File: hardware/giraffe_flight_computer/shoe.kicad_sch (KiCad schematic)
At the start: 65 parts, among them J8 USB, J9 EXT_AUDIO, U10 PCM2902C, U11 TPS61033, U12 ISO6720B, U14 74LVC1G04, U15 TLP185, U16 TLP185, Y1 12MHz

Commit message: first round of updates to telemetry board
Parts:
- removed C38: 10μF, Capacitor_Tantalum_SMD:CP_EIA-3216-18_Kemet-A, symbol Device:C_Polarized_Small
- removed C45: 100μF, Capacitor_Tantalum_SMD:CP_EIA-7343-31_Kemet-D, symbol Device:C_Polarized_Small
- removed L2: 0.47uH, Inductor_SMD:L_Coilcraft_XAL4020-XXX, symbol Device:L_Small
- removed R19: ?k, Potentiometer_SMD:Potentiometer_Bourns_TC33X_Vertical, symbol giraffe_symbols:R_Potentiometer
- removed R20: ?Ω, Resistor_SMD:R_0603_1608Metric, symbol Device:R_Small
- removed R33, R35: ?k, Resistor_SMD:R_0603_1608Metric, symbol Device:R_Small
- removed R40, R41: ?, Resistor_SMD:R_0603_1608Metric, symbol Device:R_Small
- removed TP9: ~, TestPoint:TestPoint_Pad_1.0x1.0mm, symbol Connector:TestPoint_Alt
- removed U11: TPS61033, Package_TO_SOT_SMD:SOT-583-8, symbol giraffe_symbols:TPS61033
- added C12: 10μF, Capacitor_Tantalum_SMD:CP_EIA-3216-18_Kemet-A, symbol Device:C_Polarized_Small
- added C23: 100μF, Capacitor_Tantalum_SMD:CP_EIA-7343-31_Kemet-D, symbol Device:C_Polarized_Small
- added TP1: 3v3, symbol Connector:TestPoint
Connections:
- net +BATT is gone; now on net S_5V: C25.1
- net S_3V3: now also TP1.1
- net S_4V: no longer C32.1, C41.2, C42.2, C43.2, R39.2, R44.1, TX1.8 (VBAT), U12.8 (VCC2)
- net S_5V: now also C32.1, C41.2, C42.2, C43.2, R39.2, R44.1, TX1.8 (VBAT), U12.8 (VCC2), C12.1, C23.1
- net S_GND: now also C12.2, C23.2
- no-connect marks 2 -> 0
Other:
- note removed: "Boost Converter"
- note removed: "Current Sensor"
- moved on the sheet: C25, LED3, R44, TP2

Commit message: lower flight computer board schematic complete
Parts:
- removed L5: 56uH, giraffe_flight_computer_footprints:Murata-LQH3NPH_ME-0-0-MFG, symbol Device:L_Small
- removed R42: ?k, Resistor_SMD:R_0603_1608Metric, symbol Device:R_Small
- removed R43, R44, R45, R46, R47: ?Ω, Resistor_SMD:R_0603_1608Metric, symbol Device:R_Small
- removed R48: 0Ω, Resistor_SMD:R_0603_1608Metric, symbol Device:R_Small
- removed RV2: 100k, Potentiometer_SMD:Potentiometer_Bourns_TC33X_Vertical, symbol giraffe_symbols:R_Potentiometer
- removed U14: 74LVC1G04, Package_TO_SOT_SMD:SOT-353_SC-70-5, symbol giraffe_symbols:74LVC1G04
- removed U15, U16: TLP185, Package_SO:SOIC-4_4.55x3.7mm_P2.54mm, symbol Isolator:TLP185
- added C38: 20pF, Capacitor_SMD:C_0603_1608Metric, symbol Device:C_Small
- added C45: 36pF, Capacitor_SMD:C_0603_1608Metric, symbol Device:C_Small
- added K1: TLP241A, Package_DIP:DIP-4_W8.89mm_SMDSocket_LongPads, symbol giraffe_symbols:TLP241A
- added L2: 56uH, giraffe_flight_computer_footprints:Murata-LQH3NPH_ME-0-0-MFG, symbol Device:L_Small
- added R19, R20, R31, R33, R34: ?Ω, Resistor_SMD:R_0603_1608Metric, symbol Device:R_Small
- added R21, R35, R36, R37, R38, R40: 0Ω, Resistor_SMD:R_0603_1608Metric, symbol Device:R_Small
- added RV3: 100k, Potentiometer_SMD:Potentiometer_Bourns_TC33X_Vertical, symbol giraffe_symbols:R_Potentiometer
- added TP4, TP5, TP6, TP7, TP8, TP9: TestPoint, TestPoint:TestPoint_Pad_D1.0mm, symbol Connector:TestPoint
- added U11, U6: TLP185, Package_SO:SOIC-4_4.55x3.7mm_P2.54mm, symbol Isolator:TLP185
- added U13: 74LVC1G04, Package_TO_SOT_SMD:SOT-353_SC-70-5, symbol giraffe_symbols:74LVC1G04
- AE1: value ~ -> ANT
- C12: value 10μF -> 100μF; footprint Capacitor_Tantalum_SMD:CP_EIA-3216-18_Kemet-A -> Capacitor_Tantalum_SMD:CP_EIA-7343-31_Kemet-D
- C23: value 100μF -> 10μF; footprint Capacitor_Tantalum_SMD:CP_EIA-7343-31_Kemet-D -> Capacitor_Tantalum_SMD:CP_EIA-3216-18_Kemet-A
- C44: value 20pF -> 36pF
- C46: value 36pF -> 20pF
- C47: value 36pF -> ?; footprint Capacitor_SMD:C_0603_1608Metric -> Resistor_SMD:R_0805_2012Metric; now not fitted
- C48: value 20pF -> ?; footprint Capacitor_SMD:C_0603_1608Metric -> Resistor_SMD:R_0805_2012Metric; now not fitted
- L3: value 56uH -> 68uH
- L4: value 68uH -> 56uH
- R39: value 10kΩ -> 0Ω
- TP1: footprint (none) -> TestPoint:TestPoint_Pad_D1.0mm
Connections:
- net AUDIO_IN_LEFT: now also RV3.2, TP7.1
- net AUDIO_OUT_LEFT: now also R38.1, TP8.1; no longer RV1.3
- net SA868_PTT: now also R34.2
- net SA868_PWR_CTRL: now also R19.1
- net S_3V3: now also U6.6
- net S_5V: now also K1.3 (Drain), R20.1, R37.2, TP4.1, TP5.1, U11.6, U13.5 (VCC); no longer R39.2
- net S_GND: now also C38.2, C45.2, K1.2 (Cathode), R36.1, RV3.1, U11.3, U13.3 (GND), U6.3
- net SA868 RX: now reaches TX1.1 (SQ)
- net SA868 RX: now also R21.2, R40.2
- net at LED3.2 (A): now also R20.2
- net at C48.1: now also R39.2, RV3.3; no longer AE1.1 (A)
- net at L3.2, L4.1: now also C45.1; no longer C46.1
- net SA868 PTT: now reaches TX1.5 (PTT)
- net SA868 PTT: now also R35.2
- net at LED5.2 (A): now also R33.2
- net SA868 UART RXD: now reaches TX1.16 (RXD), U12.6 (OUTB)
- net SA868 UART TXD: now reaches TX1.17 (TXD), U12.7 (INA)
- net SA868 AUDIO_OUT: now reaches TX1.3 (AF_OUT)
- net SA868 AUDIO_OUT: now also R39.1, TP9.1
- net at C47.1: now also RV1.3, R38.2; no longer L4.2
- net at C44.1, L3.1: now also L2.2; no longer TX1.12 (ANT)
- net at TX1.6 (PD): now also R37.1; no longer R39.1
- net at LED4.2 (A): now also R31.2
- net SA868 MIC_IN: now reaches RV1.2, TX1.18 (MIC_IN)
- net SA868 MIC_IN: now also TP6.1
- net at TX1.7 (H/L): now also R36.2
- new net: R35.1, U13.4
- new net: R21.1, U6.1
- new net: R33.1, U11.4, U13.2
- new net: K1.1 (Anode), R19.2
- new net: AE1.1 (A), C46.1, L4.2
- new net: R34.1, U11.1
- new net RX_DETECT: R31.1, R40.1, U6.4
- new net SA868 RF: C38.1, L2.1, TX1.12 (ANT)
- new net S_5V_IN: K1.4 (Drain)
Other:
- note added: "Optional Bulk Capacitance"
- note added: "PCM2902 USB Codec"
- note added: "PCM2902/DRA868 Audio Leveling & Filtering"
- note added: "Power Control"
- note added: "SA868 PTT Control"
- note added: "SA868 Squelch Detect"
- note added: "SA868 UART Isolation"
- note added: "SA868 VHF Radio Module"
- title: (none) -> Giraffe Flight Computer Shoe
- moved on the sheet: C24, C26, C27, C28, C29, C30, C31, C32, C33, C34, C35, C36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

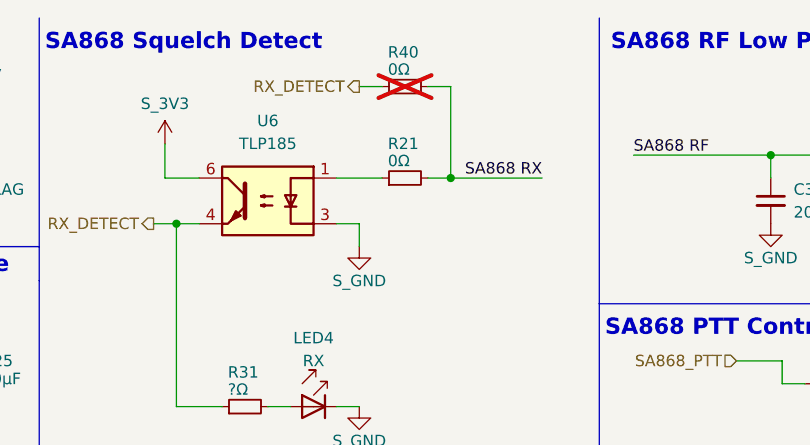
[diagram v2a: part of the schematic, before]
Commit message: 5v buck supply bom and r sense
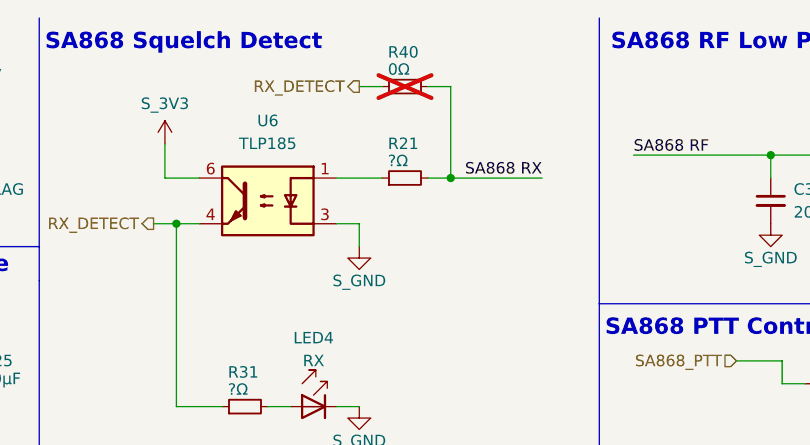
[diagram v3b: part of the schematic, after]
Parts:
- R21: value 0Ω -> ?Ω
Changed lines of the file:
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@@
 			)
 		)
-		(property "Value" "0Ω"
+		(property "Value" "?Ω"
 			(at 153.035 28.575 90)
 			(effects

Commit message: reorganization
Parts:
- removed C24, C31, C33, C34, C35, C36, C37: 1μF, Resistor_SMD:R_0805_2012Metric, symbol Device:C_Small
- removed C26: 1μF, Capacitor_SMD:C_0603_1608Metric, symbol Device:C_Small
- removed C27, C29: 10μF, Resistor_SMD:R_1210_3225Metric, symbol Device:C_Polarized_Small
- removed C30: 1uF, Resistor_SMD:R_0805_2012Metric, symbol Device:C_Small
- removed C39, C40: 0.1μF, Resistor_SMD:R_0805_2012Metric, symbol Device:C_Small
- removed J8: USB, Connector_PinHeader_1.00mm:PinHeader_1x03_P1.00mm_Vertical, symbol Connector_Generic:Conn_01x03
- removed J9: EXT_AUDIO, Connector_PinHeader_1.00mm:PinHeader_1x03_P1.00mm_Vertical, symbol Connector_Generic:Conn_01x03
- removed LED4: RX, LED_SMD:LED_0603_1608Metric, symbol giraffe_symbols:Generic_LED
- removed R28, R29: 22Ω, Resistor_SMD:R_0603_1608Metric, symbol Device:R_Small
- removed R30: 1.5kΩ, Resistor_SMD:R_0603_1608Metric, symbol Device:R_Small
- removed R31: ?Ω, Resistor_SMD:R_0603_1608Metric, symbol Device:R_Small
- removed R32: 1MΩ, Resistor_SMD:R_0603_1608Metric, symbol Device:R_Small
- removed U10: PCM2902C, Package_SO:SSOP-28_5.3x10.2mm_P0.65mm, symbol giraffe_symbols:PCM2902
- removed U13: 74LVC1G04, Package_TO_SOT_SMD:SOT-353_SC-70-5, symbol giraffe_symbols:74LVC1G04
- removed Y1: 12MHz, Crystal:Crystal_SMD_0603-2Pin_6.0x3.5mm, symbol giraffe_symbols:Crystal
- added LED6: ~, LED_SMD:LED_0603_1608Metric, symbol giraffe_symbols:Generic_LED
- added Q1, Q2, Q4: BC847CT, symbol Simulation_SPICE:NPN
- added R41: 470Ω, Resistor_SMD:R_0603_1608Metric, symbol Device:R_Small
- added R42: 5kΩ, Resistor_SMD:R_0603_1608Metric, symbol Device:R_Small
- added R43: 50kΩ, Resistor_SMD:R_0603_1608Metric, symbol Device:R_Small
- added R44: 10kΩ, Resistor_SMD:R_0603_1608Metric, symbol Device:R_Small
- added R45: 1kΩ, Resistor_SMD:R_0603_1608Metric, symbol Device:R_Small
- added R46: 390Ω, Resistor_SMD:R_0603_1608Metric, symbol Device:R_Small
- L2, L4: value 56uH -> 56nH
- L3: value 68uH -> 68nH
- LED5: value PTT -> ~
- R19: value ?Ω -> 50kΩ
- R20, R33: value ?Ω -> 150Ω
- R21: value ?Ω -> 5kΩ
- R34: value ?Ω -> 390Ω
- R40: value 0Ω -> ?kΩ; now fitted
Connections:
- net SA868 RX: no longer R40.2
- net S_3V3: now also R44.1; no longer U6.6
- net S_5V: now also R33.2, R36.2, R40.2, U11.1, R42.1, R46.1; no longer R37.2, U11.6
- net S_5V_IN: now also K1.1 (Anode)
- net S_GND: now also R37.1, U11.4, U6.4, Q1.3 (E), Q2.3 (E), Q4.3 (E); no longer K1.2 (Cathode), LED5.1 (K), R36.1, U11.3, U6.3
- net at R35.1: now also LED5.1 (K), U11.6, R42.2
- net at R21.1: now also Q4.2 (B); no longer U6.1
- net at TX1.6 (PD): now also R36.1; no longer R37.1
- net at LED5.2 (A): now also R33.1; no longer R33.2
- net at TX1.7 (H/L): now also R37.2; no longer R36.2
- net at R19.2: now also Q1.2 (B); no longer K1.1 (Anode)
- net at R34.1: now also U11.3; no longer U11.1
- net AUDIO_OUT_LEFT renamed USB Audio Codec/audio_codec_out_left
- net RX_DETECT: no longer names the net of R40.1
- net RX_DETECT: now also LED6.2 (A); no longer U6.4
- net SA868_PTT: no longer names the net of R34.2
- net SA868_PTT: now also Q2.1 (C)
- net SA868_PWR_CTRL renamed PI_GPIO_SHOE_POWER_CONTROL
- new net: R44.2, R45.2, U6.6
- new net: LED6.1 (K), Q4.1 (C), U6.3
- new net: Q2.2 (B), R43.2
- new net: Q1.1 (C), R41.2
- new net: K1.2 (Cathode), R41.1
- new net: R46.2, U6.1
- new net PI_GPIO_SA868_PTT: R43.1
- new net PI_GPIO_SA868_RX: R45.1
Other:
- added sheet USB Audio Codec (usb_audio_codec.kicad_sch)
- note added: "Basic Nets"
- note removed: "PCM2902 USB Codec"
- note removed: "Power LED"
- moved on the sheet: C38, C44, C45, C46, C47, C48, K1, L2, L3, L4, R38, R39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

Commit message: sync pcb work
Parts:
- C28, C32: footprint Resistor_SMD:R_0805_2012Metric -> Resistor_SMD:R_0603_1608Metric
- L2, L3, L4: footprint giraffe_flight_computer_footprints:Murata-LQH3NPH_ME-0-0-MFG -> Inductor_SMD:L_0603_1608Metric_Pad1.05x0.95mm_HandSolder
- Q1, Q2, Q4: footprint (none) -> Package_TO_SOT_SMD:SOT-23; symbol Simulation_SPICE:NPN -> giraffe_symbols:BC847AT
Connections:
- net S_5V: no longer C12.1, C23.1, C25.1
- net S_5V_IN: now also C12.1, C23.1, C25.1
- net S_GND: now also Q1.2 (E), Q2.2 (E), Q4.2 (E); no longer Q1.3 (E), Q2.3 (E), Q4.3 (E)
- net at R34.2: now also Q2.3 (C); no longer Q2.1 (C)
- net at LED6.1 (K), U6.3: now also Q4.3 (C); no longer Q4.1 (C)
- net at R21.1: now also Q4.1 (B); no longer Q4.2 (B)
- net at R43.2: now also Q2.1 (B); no longer Q2.2 (B)
- net at Q1.1 (B): now also R19.2; no longer R41.2
- new net: Q1.3 (C), R41.2
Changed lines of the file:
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@@
 	)
 	(junction
-		(at 128.27 43.18)
-		(diameter 0)
-		(color 0 0 0 0)
-	)
-	(junction
 		(at 87.63 158.75)
 		(diameter 0)
@@
 	(wire
 		(pts
-			(xy 128.27 49.53) (xy 129.54 49.53)
+			(xy 125.73 49.53) (xy 129.54 49.53)
 		)
 		(stroke
@@
 	(wire
 		(pts
-			(xy 128.27 43.18) (xy 128.27 49.53)
-		)
-		(stroke
-			(width 0)
-			(type default)
-		)
-	)
-	(wire
-		(pts
 			(xy 172.72 43.18) (xy 168.91 43.18)
 		)
@@
 		)
 	)
+	(hierarchical_label "S_5V_IN"
+		(shape input)
+		(at 125.73 49.53 180)
+		(fields_autoplaced yes)
+		(effects
+			(font
+				(size 1.27 1.27)
+			)
+			(justify right)
+		)
+	)
 	(netclass_flag ""
 		(length 2.54)
@@
 		)
 	)
+	(netclass_flag ""
+		(length 2.54)
+		(shape round)
+		(at 190.5 30.48 0)
+		(fields_autoplaced yes)
+		(effects
+			(font
+				(size 1.27 1.27)
+			)
+			(justify left bottom)
+		)
+		(property "Netclass" "RF"
+			(at 191.008 27.94 0)
+			(effects
+				(font
+					(size 1.27 1.27)
+					(italic yes)
+				)
+				(justify left)
+			)
+		)
+	)
 	(symbol
 		(lib_id "Device:C_Small")
@@
 			)
 		)
-		(property "Footprint" "giraffe_flight_computer_footprints:Murata-LQH3NPH_ME-0-0-MFG"
+		(property "Footprint" "Inductor_SMD:L_0603_1608Metric_Pad1.05x0.95mm_HandSolder"
 			(at 218.44 30.48 0)
 			(effects
@@
 	)
 	(symbol
-		(lib_id "Simulation_SPICE:NPN")
+		(lib_id "giraffe_symbols:BC847AT")
 		(at 135.89 99.06 0)
 		(mirror y)
@@
 			)
 		)
-		(property "Footprint" ""
+		(property "Footprint" "Package_TO_SOT_SMD:SOT-23"
 			(at 72.39 99.06 0)
 			(effects
@@
 	)
 	(symbol
-		(lib_id "Simulation_SPICE:NPN")
+		(lib_id "giraffe_symbols:BC847AT")
 		(at 77.47 50.8 0)
 		(unit 1)
@@
 			)
 		)
-		(property "Footprint" ""
+		(property "Footprint" "Package_TO_SOT_SMD:SOT-23"
 			(at 140.97 50.8 0)
 			(effects
@@
 			)
 		)
-		(property "Footprint" "giraffe_flight_computer_footprints:Murata-LQH3NPH_ME-0-0-MFG"
+		(property "Footprint" "Inductor_SMD:L_0603_1608Metric_Pad1.05x0.95mm_HandSolder"
 			(at 233.68 30.48 0)
 			(effects
@@
 			)
 		)
-		(property "Footprint" "Resistor_SMD:R_0805_2012Metric"
+		(property "Footprint" "Resistor_SMD:R_0603_1608Metric"
 			(at 22.86 83.82 0)
 			(effects
@@
 			)
 		)
-		(property "Footprint" "Resistor_SMD:R_0805_2012Metric"
+		(property "Footprint" "Resistor_SMD:R_0603_1608Metric"
 			(at 64.77 83.82 0)
 			(effects
@@
 			)
 		)
-		(property "Footprint" "giraffe_flight_computer_footprints:Murata-LQH3NPH_ME-0-0-MFG"
+		(property "Footprint" "Inductor_SMD:L_0603_1608Metric_Pad1.05x0.95mm_HandSolder"
 			(at 203.2 30.48 0)
 			(effects
@@
 	)
 	(symbol
-		(lib_id "Simulation_SPICE:NPN")
+		(lib_id "giraffe_symbols:BC847AT")
 		(at 199.39 93.98 0)
 		(unit 1)
@@
 			)
 		)
-		(property "Footprint" ""
+		(property "Footprint" "Package_TO_SOT_SMD:SOT-23"
 			(at 262.89 93.98 0)
 			(effects
@@
 		)
 		(property "Description" "Bipolar transistor symbol for simulation only, substrate tied to the emitter"
-			(at 199.39 93.98 0)
+			(at 189.23 88.9 0)
 			(effects
 				(font
@@
 		)
 		(property "Sim.Type" "GUMMELPOON"
-			(at 199.39 93.98 0)
+			(at 196.85 88.9 0)
 			(effects
 				(font
@@
 		)
 		(property "Sim.Pins" "1=C 2=B 3=E"
-			(at 199.39 93.98 0)
+			(at 196.85 88.9 0)
 			(effects
 				(font

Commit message: Packages, complete PCBs, Map, Install Structure
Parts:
- removed Q4: BC847CT, Package_TO_SOT_SMD:SOT-23, symbol giraffe_symbols:BC847AT
- removed R21: 5kΩ, Resistor_SMD:R_0603_1608Metric, symbol Device:R_Small
- removed R34: 390Ω, Resistor_SMD:R_0603_1608Metric, symbol Device:R_Small
- removed R38, R39: 0Ω, Resistor_SMD:R_0603_1608Metric, symbol Device:R_Small
- removed R44: 10kΩ, Resistor_SMD:R_0603_1608Metric, symbol Device:R_Small
- removed R45: 1kΩ, Resistor_SMD:R_0603_1608Metric, symbol Device:R_Small
- removed TP1: 3v3, TestPoint:TestPoint_Pad_D1.0mm, symbol Connector:TestPoint
- removed U11, U6: TLP185, Package_SO:SOIC-4_4.55x3.7mm_P2.54mm, symbol Isolator:TLP185
- added Q5: BC847CT, Package_TO_SOT_SMD:SOT-23, symbol giraffe_symbols:BC847AT
- added R31: 5kΩ, Resistor_SMD:R_0603_1608Metric, symbol Device:R_Small
- C12: now not fitted
- C47, C48: footprint Resistor_SMD:R_0805_2012Metric -> Resistor_SMD:R_0603_1608Metric
- R46: value 390Ω -> 5kΩ
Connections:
- net AUDIO_IN_LEFT: now also C48.1
- net PI_GPIO_SA868_RX: now also R40.2, Q5.2 (E), R31.1
- net SA868 AUDIO_OUT: now also RV3.3
- net SA868 MIC_IN: now also C47.1
- net SA868 RX: now also R46.1
- net S_3V3: now also Q5.3 (C)
- net S_5V: no longer R40.2, R46.1
- net S_GND: now also LED6.1 (K), R31.2
- net USB Audio Codec/audio_codec_out_left: now also RV1.3
- net SA868 H/L: now reaches R37.2, TX1.7 (H/L)
- net at Q2.3 (C): now also LED5.1 (K), R35.1, R42.2
- net at R46.2: now also Q5.1 (B)
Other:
- moved on the sheet: C47, C48, LED6, R37, R40, RV1, RV3
